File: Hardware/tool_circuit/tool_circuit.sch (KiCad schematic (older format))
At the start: 0 parts

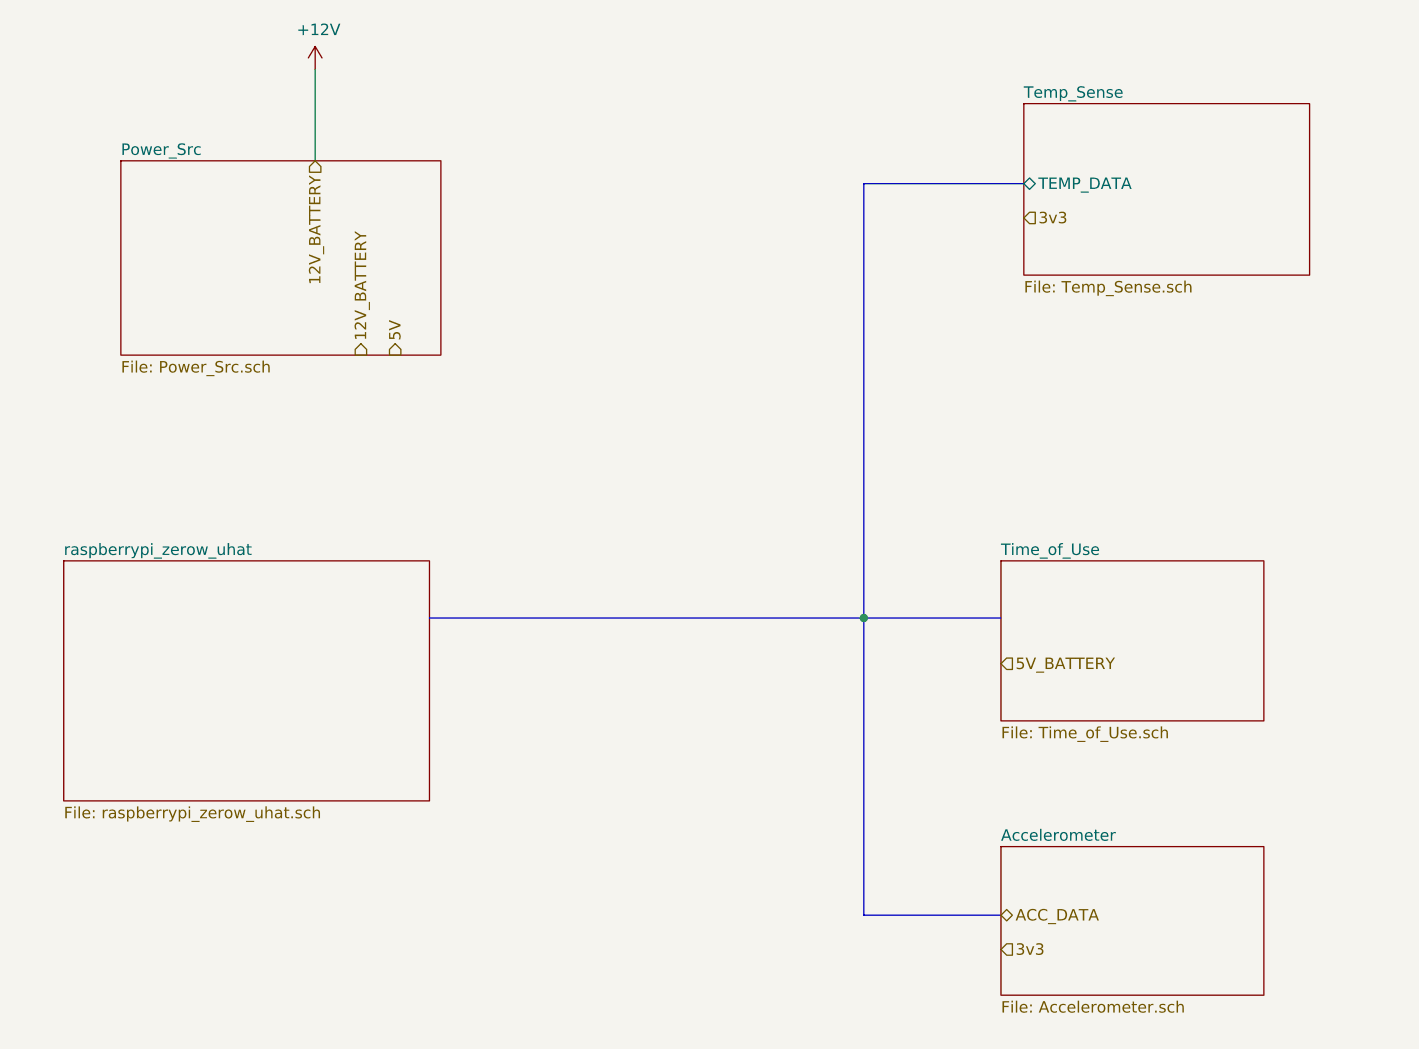
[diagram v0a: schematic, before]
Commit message: Tool Circuit schematic updates
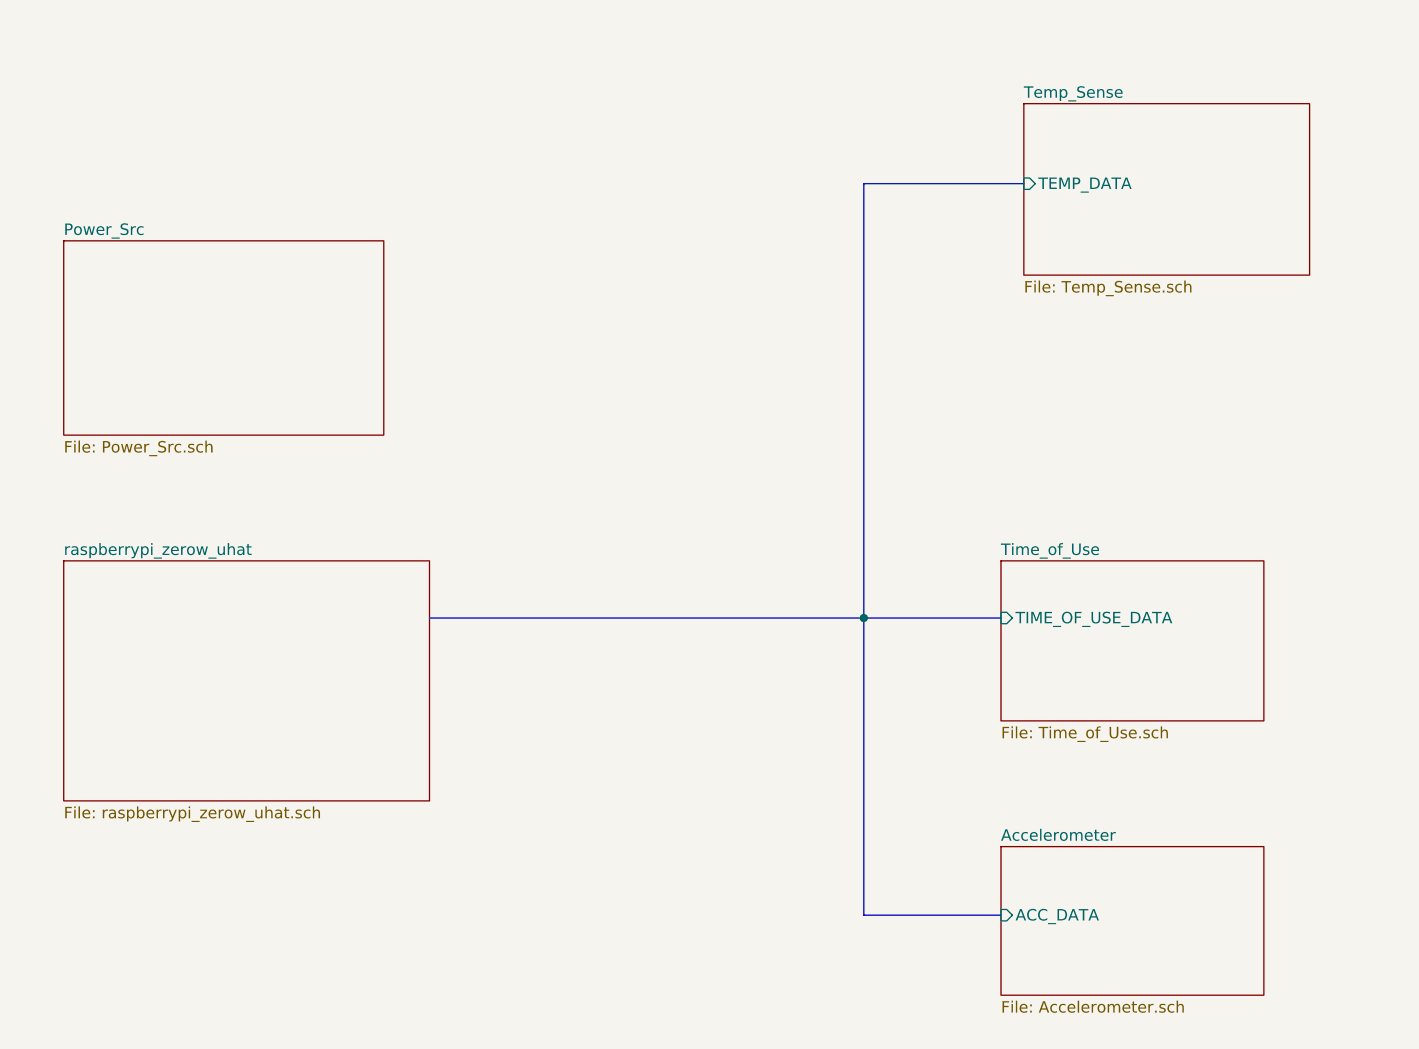
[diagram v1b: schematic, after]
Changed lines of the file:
@@
 $Descr A4 11693 8268
 encoding utf-8
-Sheet 1 7
+Sheet 1 8
 Title ""
 Date ""
@@
 Comment4 ""
 $EndDescr
+Wire Bus Line
+	3350 4450 5250 4450
+Wire Bus Line
+	5950 2550 5250 2550
+$Sheet
+S 1750 2800 1400 850
+U 611DBAE9
+F0 "Power_Src" 50
+F1 "Power_Src.sch" 50
+$EndSheet
+Connection ~ 5250 4450
+$Sheet
+S 1750 4200 1600 1050
+U 61460B87
+F0 "raspberrypi_zerow_uhat" 50
+F1 "raspberrypi_zerow_uhat.sch" 50
+$EndSheet
+Wire Bus Line
+	5250 4450 5250 5750
+Wire Bus Line
+	5250 5750 5850 5750
+$Sheet
+S 5850 5450 1150 650
+U 61495548
+F0 "Accelerometer" 50
+F1 "Accelerometer.sch" 50
+F2 "ACC_DATA" I L 5850 5750 50
+$EndSheet
 $Sheet
 S 5850 4200 1150 700
@@
 F0 "Time_of_Use" 50
 F1 "Time_of_Use.sch" 50
-$EndSheet
-Wire Bus Line
-	3350 4450 5250 4450
-Wire Bus Line
-	5950 2550 5250 2550
-Wire Bus Line
-	5250 4450 5850 4450
-$Comp
-L power:+12V #PWR0101
-U 1 1 6125A008
-P 2850 2050
-F 0 "#PWR0101" H 2850 1900 50  0001 C CNN
-F 1 "+12V" H 2865 2223 50  0000 C CNN
-F 2 "" H 2850 2050 50  0001 C CNN
-F 3 "" H 2850 2050 50  0001 C CNN
-	1    2850 2050
-	1    0    0    -1
-$EndComp
-Text HLabel 2850 2450 3    50   Input ~ 0
-12V_BATTERY
-Wire Wire Line
-	2850 2050 2850 2450
-Text HLabel 3050 3300 1    50   Output ~ 0
-12V_BATTERY
-Text HLabel 3200 3300 1    50   Output ~ 0
-5V
-$Sheet
-S 2000 2450 1400 850
-U 611DBAE9
-F0 "Power_Src" 50
-F1 "Power_Src.sch" 50
+F2 "TIME_OF_USE_DATA" I L 5850 4450 50
 $EndSheet
 $Sheet
@@
 F0 "Temp_Sense" 50
 F1 "Temp_Sense.sch" 50
-F2 "TEMP_DATA" B L 5950 2550 50
+F2 "TEMP_DATA" I L 5950 2550 50
 $EndSheet
-Connection ~ 5250 4450
 Wire Bus Line
 	5250 2550 5250 4450
-$Sheet
-S 1750 4200 1600 1050
-U 61460B87
-F0 "raspberrypi_zerow_uhat" 50
-F1 "raspberrypi_zerow_uhat.sch" 50
-$EndSheet
-$Sheet
-S 5850 5450 1150 650
-U 61495548
-F0 "Accelerometer" 50
-F1 "Accelerometer.sch" 50
-$EndSheet
 Wire Bus Line
-	5250 4450 5250 5750
-Wire Bus Line
-	5250 5750 5850 5750
-Text HLabel 5850 5750 2    50   BiDi ~ 0
-ACC_DATA
-Text HLabel 5950 2700 2    50   Input ~ 0
-3v3
-Text HLabel 5850 4650 2    50   Input ~ 0
-5V_BATTERY
-Text HLabel 5850 5900 2    50   Input ~ 0
-3v3
+	5250 4450 5850 4450
 $EndSCHEMATC

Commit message: schematic revisions
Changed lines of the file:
@@
 $EndSheet
 Connection ~ 5250 4450
-$Sheet
-S 1750 4200 1600 1050
-U 61460B87
-F0 "raspberrypi_zerow_uhat" 50
-F1 "raspberrypi_zerow_uhat.sch" 50
-$EndSheet
 Wire Bus Line
 	5250 4450 5250 5750
-Wire Bus Line
-	5250 5750 5850 5750
-$Sheet
-S 5850 5450 1150 650
-U 61495548
-F0 "Accelerometer" 50
-F1 "Accelerometer.sch" 50
-F2 "ACC_DATA" I L 5850 5750 50
-$EndSheet
 $Sheet
 S 5850 4200 1150 700
@@
 Wire Bus Line
 	5250 4450 5850 4450
+$Sheet
+S 5900 5500 1150 650
+U 61514F06
+F0 "Accelerometer.sch" 50
+F1 "Accelerometer.sch" 50
+F2 "ACC_DATA" I L 5900 5750 50
+$EndSheet
+$Sheet
+S 1550 4400 1800 900
+U 61514F71
+F0 "raspberrypi_header.sch" 50
+F1 "raspberrypi_header.sch" 50
+$EndSheet
+Wire Bus Line
+	5250 5750 5900 5750
 $EndSCHEMATC

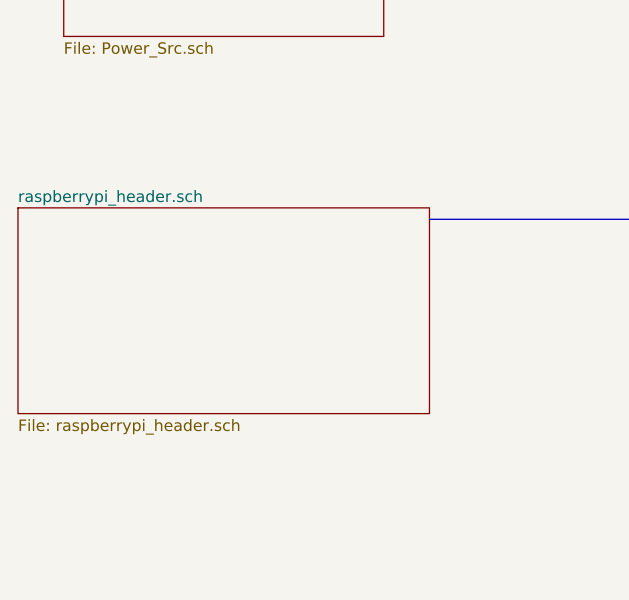
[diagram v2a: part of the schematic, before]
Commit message: schematic LEDs + switch
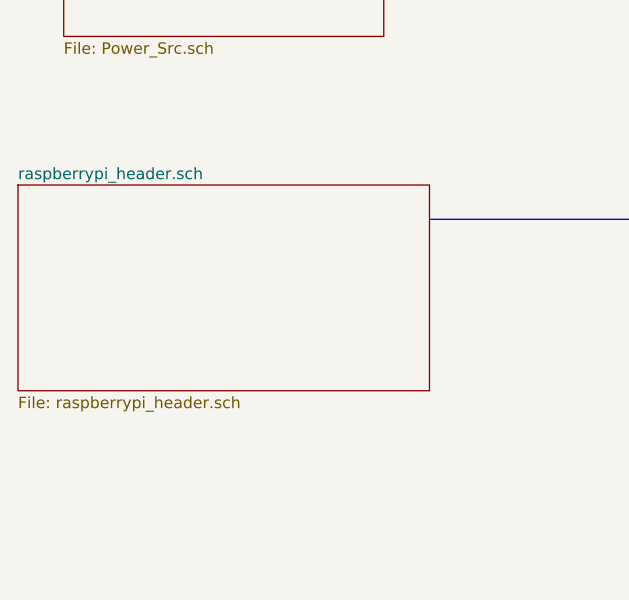
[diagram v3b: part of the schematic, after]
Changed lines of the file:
@@
 F2 "ACC_DATA" I L 5900 5750 50
 $EndSheet
+Wire Bus Line
+	5250 5750 5900 5750
 $Sheet
-S 1550 4400 1800 900
+S 1550 4300 1800 900
 U 61514F71
 F0 "raspberrypi_header.sch" 50
 F1 "raspberrypi_header.sch" 50
 $EndSheet
-Wire Bus Line
-	5250 5750 5900 5750
 $EndSCHEMATC

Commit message: made some post review changes
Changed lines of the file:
@@
 $EndDescr
-Wire Bus Line
-	3350 4450 5250 4450
 Wire Bus Line
 	5950 2550 5250 2550
@@
 Connection ~ 5250 4450
 Wire Bus Line
-	5250 4450 5250 5750
+	5250 4450 5250 4550
 $Sheet
 S 5850 4200 1150 700
@@
 F0 "Time_of_Use" 50
 F1 "Time_of_Use.sch" 50
-F2 "TIME_OF_USE_DATA" I L 5850 4450 50
+F2 "TIME_OF_USE_DATA" B L 5850 4450 50
 $EndSheet
 $Sheet
@@
 F0 "Temp_Sense" 50
 F1 "Temp_Sense.sch" 50
-F2 "TEMP_DATA" I L 5950 2550 50
+F2 "TEMP_DATA" B L 5950 2550 50
 $EndSheet
 Wire Bus Line
@@
 F0 "Accelerometer.sch" 50
 F1 "Accelerometer.sch" 50
-F2 "ACC_DATA" I L 5900 5750 50
+F2 "ACC_DATA" B L 5900 5750 50
 $EndSheet
 Wire Bus Line
@@
 F0 "raspberrypi_header.sch" 50
 F1 "raspberrypi_header.sch" 50
+F2 "PI_CONN" B R 3350 4550 50
 $EndSheet
+Connection ~ 5250 4550
+Wire Bus Line
+	5250 4550 5250 5750
+Wire Bus Line
+	3350 4550 5250 4550
 $EndSCHEMATC

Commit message: Latest revisions to schematic
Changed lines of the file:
@@
 	5950 2550 5250 2550
 $Sheet
-S 1750 2800 1400 850
+S 2600 2350 1400 850
 U 611DBAE9
 F0 "Power_Src" 50

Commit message: schematic updates
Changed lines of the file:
@@
 	5950 2550 5250 2550
 $Sheet
-S 2600 2350 1400 850
+S 1550 2550 1400 850
 U 611DBAE9
 F0 "Power_Src" 50

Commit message: pcb revisions
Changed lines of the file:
@@
 Comment4 ""
 $EndDescr
-Wire Bus Line
-	5950 2550 5250 2550
 $Sheet
-S 1550 2550 1400 850
+S 3400 2300 1400 850
 U 611DBAE9
 F0 "Power_Src" 50
 F1 "Power_Src.sch" 50
 $EndSheet
-Connection ~ 5250 4450
-Wire Bus Line
-	5250 4450 5250 4550
 $Sheet
-S 5850 4200 1150 700
+S 6400 3750 1150 700
 U 611DF2F9
 F0 "Time_of_Use" 50
 F1 "Time_of_Use.sch" 50
-F2 "TIME_OF_USE_DATA" B L 5850 4450 50
 $EndSheet
 $Sheet
-S 5950 2200 1250 750
+S 6350 2450 1250 750
 U 611DBC89
 F0 "Temp_Sense" 50
 F1 "Temp_Sense.sch" 50
-F2 "TEMP_DATA" B L 5950 2550 50
 $EndSheet
-Wire Bus Line
-	5250 2550 5250 4450
-Wire Bus Line
-	5250 4450 5850 4450
 $Sheet
-S 5900 5500 1150 650
+S 3200 3800 1800 900
+U 61514F71
+F0 "raspberrypi_header.sch" 50
+F1 "raspberrypi_header.sch" 50
+$EndSheet
+$Sheet
+S 6450 5050 1150 650
 U 61514F06
 F0 "Accelerometer.sch" 50
 F1 "Accelerometer.sch" 50
-F2 "ACC_DATA" B L 5900 5750 50
 $EndSheet
-Wire Bus Line
-	5250 5750 5900 5750
-$Sheet
-S 1550 4300 1800 900
-U 61514F71
-F0 "raspberrypi_header.sch" 50
-F1 "raspberrypi_header.sch" 50
-F2 "PI_CONN" B R 3350 4550 50
-$EndSheet
-Connection ~ 5250 4550
-Wire Bus Line
-	5250 4550 5250 5750
-Wire Bus Line
-	3350 4550 5250 4550
 $EndSCHEMATC
